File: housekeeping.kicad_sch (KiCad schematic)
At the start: 38 parts, among them U13 DAC53401, U15 MC34063A, U16 MC34063A

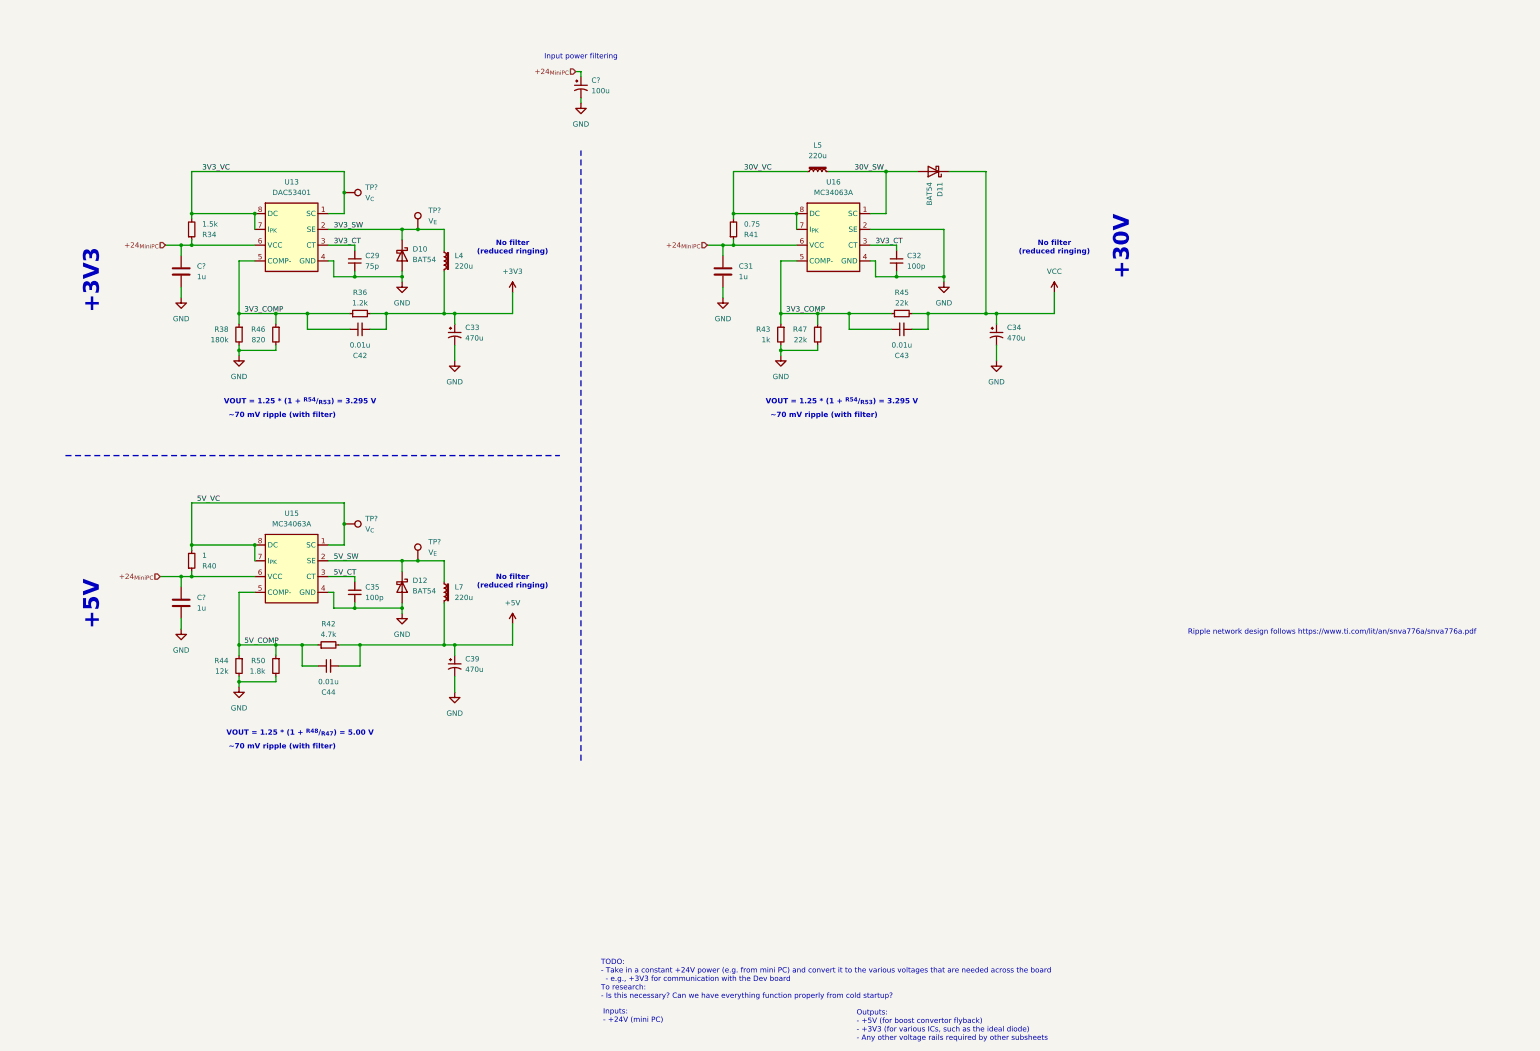
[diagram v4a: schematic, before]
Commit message: Properly spec 30V output
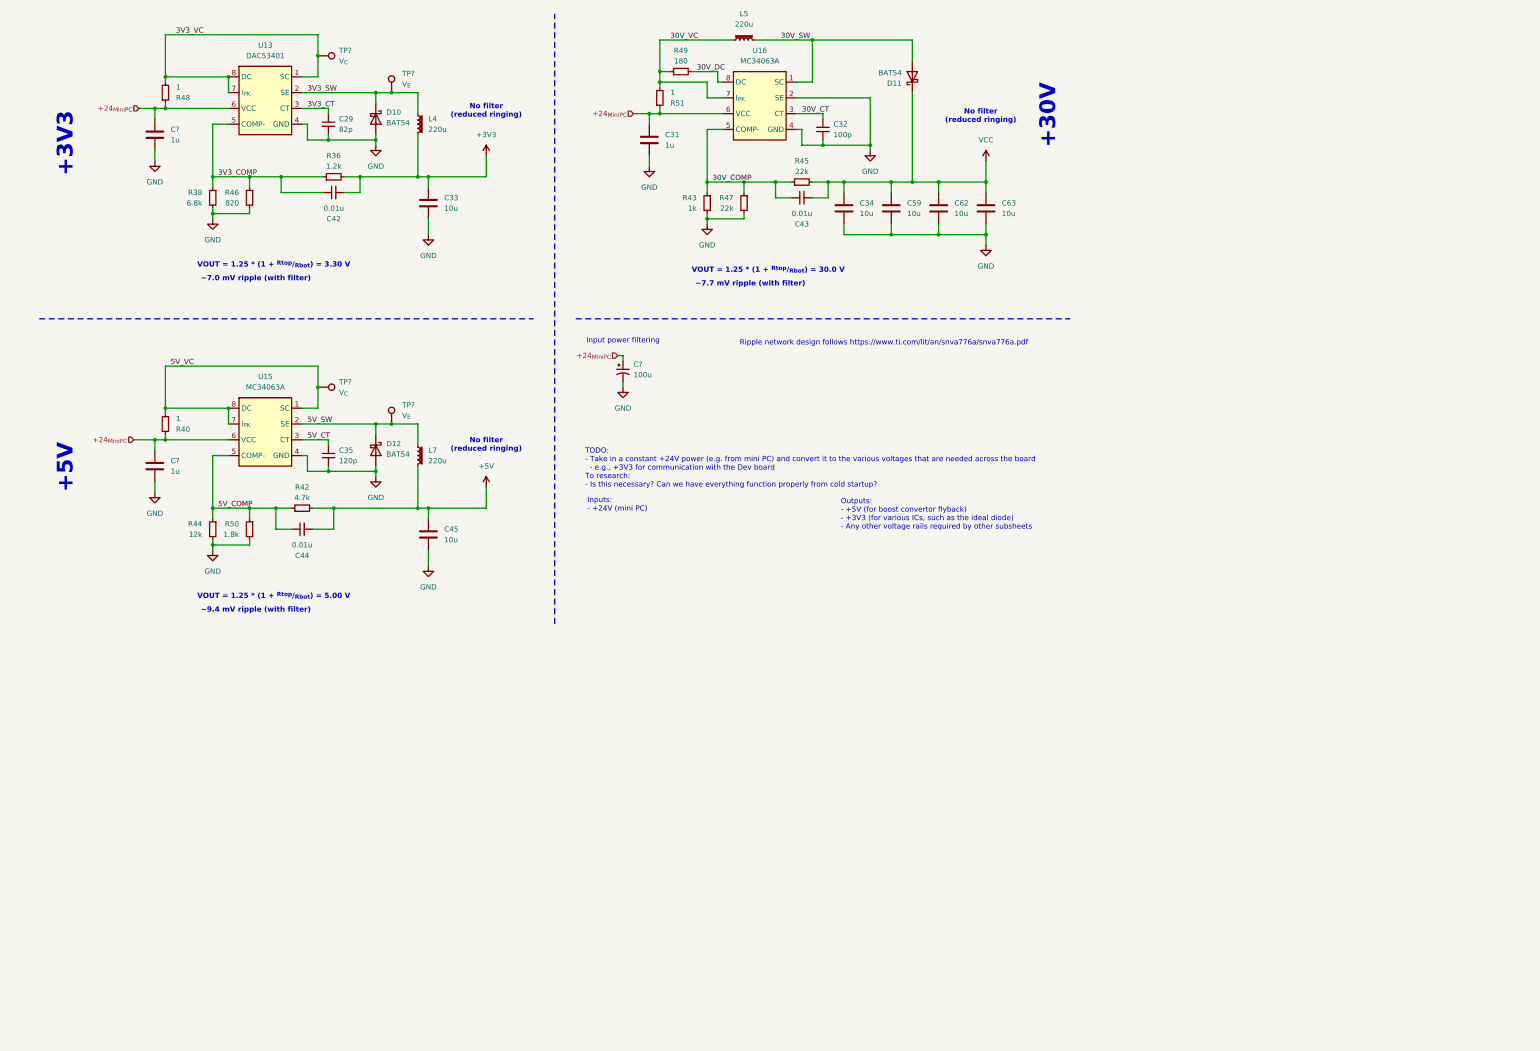
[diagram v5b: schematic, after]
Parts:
- removed C33, C34, C39: 470u, Capacitor_THT:CP_Radial_D10.0mm_P5.00mm, symbol Device:C_Polarized_Small_US
- removed R34: 1.5k, Resistor_SMD:R_0603_1608Metric_Pad0.98x0.95mm_HandSolder, symbol Device:R_Small
- removed R41: 0.75, Resistor_SMD:R_0603_1608Metric_Pad0.98x0.95mm_HandSolder, symbol Device:R_Small
- added C33, C34, C45, C59, C62, C63: 10u, Capacitor_SMD:C_0603_1608Metric_Pad1.08x0.95mm_HandSolder, symbol Device:C
- added R48, R51: 1, Resistor_SMD:R_0603_1608Metric_Pad0.98x0.95mm_HandSolder, symbol Device:R_Small
- added R49: 180, Resistor_SMD:R_0603_1608Metric_Pad0.98x0.95mm_HandSolder, symbol Device:R_Small
- C29: value 75p -> 82p
- C35: value 100p -> 120p
- R38: value 180k -> 6.8k
- R40: Mouser Part Number 667-ERJ-3RQFR33V -> 652-CR0603-F/1R00ELF
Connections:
- net +24_{MiniPC}: now also R48.1, R51.1
- net +3V3: now also C33.1
- net +5V: now also C45.1
- net 30V_VC: now also R49.1, R51.2; no longer U16.8 (DC)
- net 3V3_COMP: no longer C43.1, R43.1, R45.1, R47.1, U16.5 (COMP-)
- net 3V3_CT: no longer C32.1, U16.3 (CT)
- net 3V3_VC: now also R48.2
- net GND: now also C33.2, C34.2, C45.2, C59.2, C62.2, C63.2
- net VCC: now also C34.1, C59.1, C62.1, C63.1
- new net 30V_COMP: C43.1, R43.1, R45.1, R47.1, U16.5 (COMP-)
- new net 30V_CT: C32.1, U16.3 (CT)
- new net 30V_DC: R49.2, U16.8 (DC)
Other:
- note added: "VOUT = 1.25 * (1 + ^{Rtop}/_{Rbot}) = 3.30 V"
- note added: "VOUT = 1.25 * (1 + ^{Rtop}/_{Rbot}) = 30.0 V"
- note added: "VOUT = 1.25 * (1 + ^{Rtop}/_{Rbot}) = 5.00 V"
- note added: "~7.0 mV ripple (with filter)"
- note added: "~7.7 mV ripple (with filter)"
- note added: "~9.4 mV ripple (with filter)"
- note removed: "VOUT = 1.25 * (1 + ^{R48}/_{R47}) = 5.00 V"
- note removed: "VOUT = 1.25 * (1 + ^{R54}/_{R53}) = 3.295 V"
- note removed: "~70 mV ripple (with filter)"
- moved on the sheet: C29, C31, C32, C35, C42, C43, C44, C?, D10, D11, D12, L4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

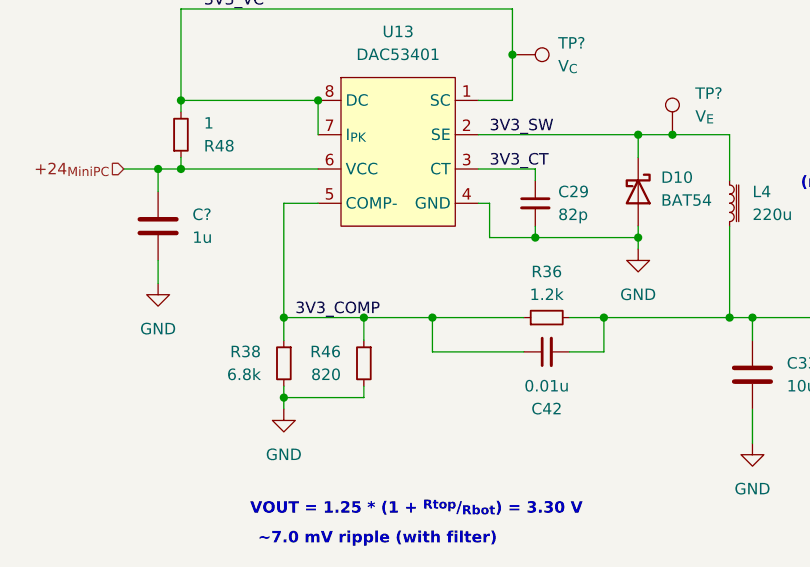
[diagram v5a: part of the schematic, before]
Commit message: Tuned circuits & adjusted values
Changed footprints for some circuits to consolidate components
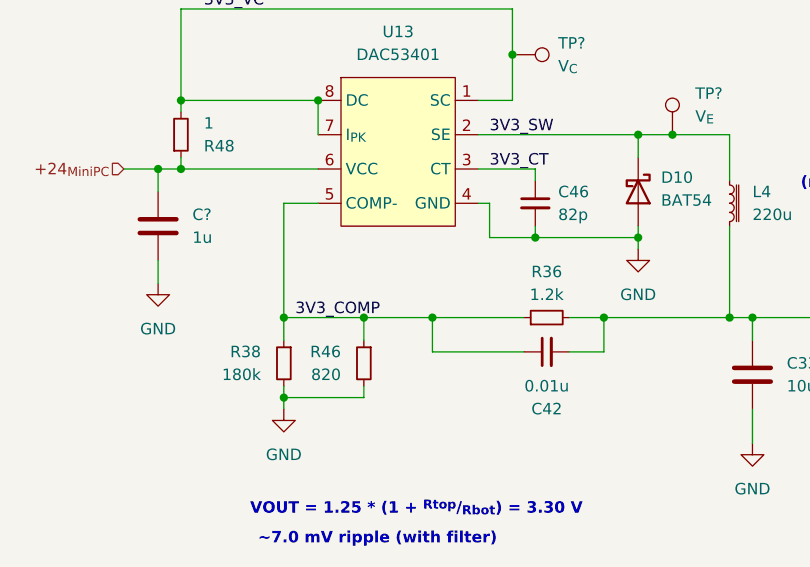
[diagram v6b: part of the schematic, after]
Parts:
- removed C29: 82p, Capacitor_SMD:C_0603_1608Metric_Pad1.08x0.95mm_HandSolder, symbol Device:C_Small
- added C46: 82p, Capacitor_SMD:C_0603_1608Metric_Pad1.08x0.95mm_HandSolder, symbol Device:C_Small
- R38: value 6.8k -> 180k
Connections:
- net 3V3_CT: now also C46.1
- net GND: now also C46.2
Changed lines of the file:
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@@
 	(title_block
 		(title "Housekeeping Power Supplies")
-		(date "2025-02-12")
-		(rev "1")
+		(date "2025-05-14")
+		(rev "2")
 		(company "UT Robomaster")
 		(comment 1 "Robomaster")
@@
 	)
 	(symbol
-		(lib_id "Device:C_Small")
-		(at 92.71 58.42 0)
-		(unit 1)
-		(exclude_from_sim no)
-		(in_bom yes)
-		(on_board yes)
-		(dnp no)
-		(fields_autoplaced yes)
-		(property "Reference" "C29"
-			(at 95.25 57.1562 0)
-			(effects
-				(font
-					(size 1.27 1.27)
-				)
-				(justify left)
-			)
-		)
-		(property "Value" "82p"
-			(at 95.25 59.6962 0)
-			(effects
-				(font
-					(size 1.27 1.27)
-				)
-				(justify left)
-			)
-		)
-		(property "Footprint" "Capacitor_SMD:C_0603_1608Metric_Pad1.08x0.95mm_HandSolder"
-			(at 92.71 58.42 0)
-			(effects
-				(font
-					(size 1.27 1.27)
-				)
-				(hide yes)
-			)
-		)
-		(property "Datasheet" "~"
-			(at 92.71 58.42 0)
-			(effects
-				(font
-					(size 1.27 1.27)
-				)
-				(hide yes)
-			)
-		)
-		(property "Description" "Unpolarized capacitor, small symbol"
-			(at 92.71 58.42 0)
-			(effects
-				(font
-					(size 1.27 1.27)
-				)
-				(hide yes)
-			)
-		)
-		(property "Sim.Device" ""
-			(at 92.71 58.42 0)
-			(effects
-				(font
-					(size 1.27 1.27)
-				)
-			)
-		)
-		(property "Sim.Pins" ""
-			(at 92.71 58.42 0)
-			(effects
-				(font
-					(size 1.27 1.27)
-				)
-			)
-		)
-		(property "Sim.Type" ""
-			(at 92.71 58.42 0)
-			(effects
-				(font
-					(size 1.27 1.27)
-				)
-			)
-		)
-		(property "Height" ""
-			(at 92.71 58.42 0)
-			(effects
-				(font
-					(size 1.27 1.27)
-				)
-			)
-		)
-		(property "Manufacturer_Name" ""
-			(at 92.71 58.42 0)
-			(effects
-				(font
-					(size 1.27 1.27)
-				)
-			)
-		)
-		(property "Manufacturer_Part_Number" ""
-			(at 92.71 58.42 0)
-			(effects
-				(font
-					(size 1.27 1.27)
-				)
-			)
-		)
-		(property "Mouser Price/Stock" ""
-			(at 92.71 58.42 0)
-			(effects
-				(font
-					(size 1.27 1.27)
-				)
-			)
-		)
-		(pin "2"
-		)
-		(pin "1"
-		)
-		(instances
-			(project "SupercapManager"
-				(path "/6197145b-e7d4-44cc-9d90-537b6501bf60/2b4de7d2-e111-42d9-afee-f810f96a2f61"
-					(reference "C29")
-					(unit 1)
-				)
-			)
-			(project "Housekeeping Rev1"
-				(path "/d2a5f610-b666-4f42-b17a-f8b6e55a52c2/25bdba42-617b-4aa1-85da-258c1454f7e3"
-					(reference "C1")
-					(unit 1)
-				)
-			)
-		)
-	)
-	(symbol
 		(lib_id "power:GND")
 		(at 50.8 147.32 0)
@@
 	)
 	(symbol
+		(lib_id "Device:C_Small")
+		(at 92.71 58.42 0)
+		(unit 1)
+		(exclude_from_sim no)
+		(in_bom yes)
+		(on_board yes)
+		(dnp no)
+		(fields_autoplaced yes)
+		(property "Reference" "C46"
+			(at 95.25 57.1562 0)
+			(effects
+				(font
+					(size 1.27 1.27)
+				)
+				(justify left)
+			)
+		)
+		(property "Value" "82p"
+			(at 95.25 59.6962 0)
+			(effects
+				(font
+					(size 1.27 1.27)
+				)
+				(justify left)
+			)
+		)
+		(property "Footprint" "Capacitor_SMD:C_0603_1608Metric_Pad1.08x0.95mm_HandSolder"
+			(at 92.71 58.42 0)
+			(effects
+				(font
+					(size 1.27 1.27)
+				)
+				(hide yes)
+			)
+		)
+		(property "Datasheet" "~"
+			(at 92.71 58.42 0)
+			(effects
+				(font
+					(size 1.27 1.27)
+				)
+				(hide yes)
+			)
+		)
+		(property "Description" "Unpolarized capacitor, small symbol"
+			(at 92.71 58.42 0)
+			(effects
+				(font
+					(size 1.27 1.27)
+				)
+				(hide yes)
+			)
+		)
+		(property "Sim.Device" ""
+			(at 92.71 58.42 0)
+			(effects
+				(font
+					(size 1.27 1.27)
+				)
+			)
+		)
+		(property "Sim.Pins" ""
+			(at 92.71 58.42 0)
+			(effects
+				(font
+					(size 1.27 1.27)
+				)
+			)
+		)
+		(property "Sim.Type" ""
+			(at 92.71 58.42 0)
+			(effects
+				(font
+					(size 1.27 1.27)
+				)
+			)
+		)
+		(property "Height" ""
+			(at 92.71 58.42 0)
+			(effects
+				(font
+					(size 1.27 1.27)
+				)
+			)
+		)
+		(property "Manufacturer_Name" ""
+			(at 92.71 58.42 0)
+			(effects
+				(font
+					(size 1.27 1.27)
+				)
+			)
+		)
+		(property "Manufacturer_Part_Number" ""
+			(at 92.71 58.42 0)
+			(effects
+				(font
+					(size 1.27 1.27)
+				)
+			)
+		)
+		(property "Mouser Price/Stock" ""
+			(at 92.71 58.42 0)
+			(effects
+				(font
+					(size 1.27 1.27)
+				)
+			)
+		)
+		(pin "2"
+		)
+		(pin "1"
+		)
+		(instances
+			(project "SupercapManager"
+				(path "/6197145b-e7d4-44cc-9d90-537b6501bf60/2b4de7d2-e111-42d9-afee-f810f96a2f61"
+					(reference "C46")
+					(unit 1)
+				)
+			)
+		)
+	)
+	(symbol
 		(lib_id "Connector:TestPoint")
 		(at 107.95 130.81 0)
@@
 			)
 		)
-		(property "Value" "6.8k"
+		(property "Value" "180k"
 			(at 62.23 77.4699 0)
 			(effects
